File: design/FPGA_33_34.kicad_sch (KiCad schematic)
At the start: 21 parts, among them Q15 SI1036X, U1 XC7K160T-2FFG676C, U42 TXS0108E

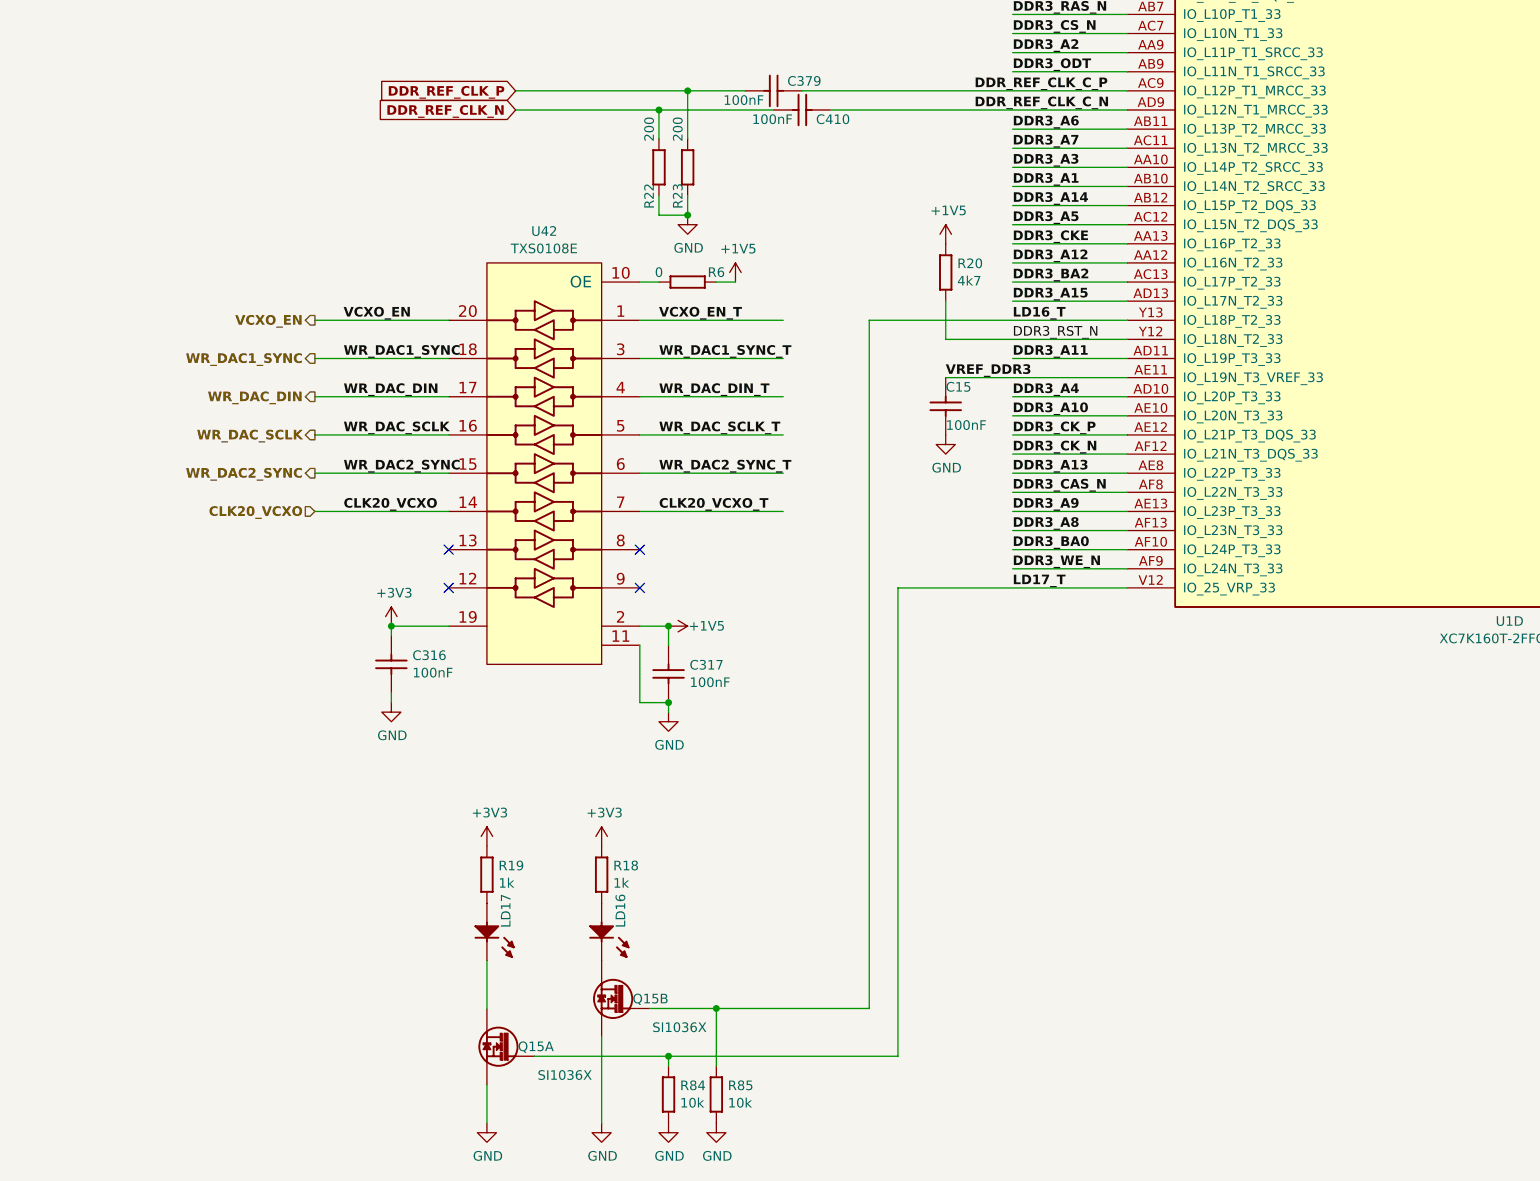
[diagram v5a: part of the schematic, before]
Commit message: new level translators
new level translators
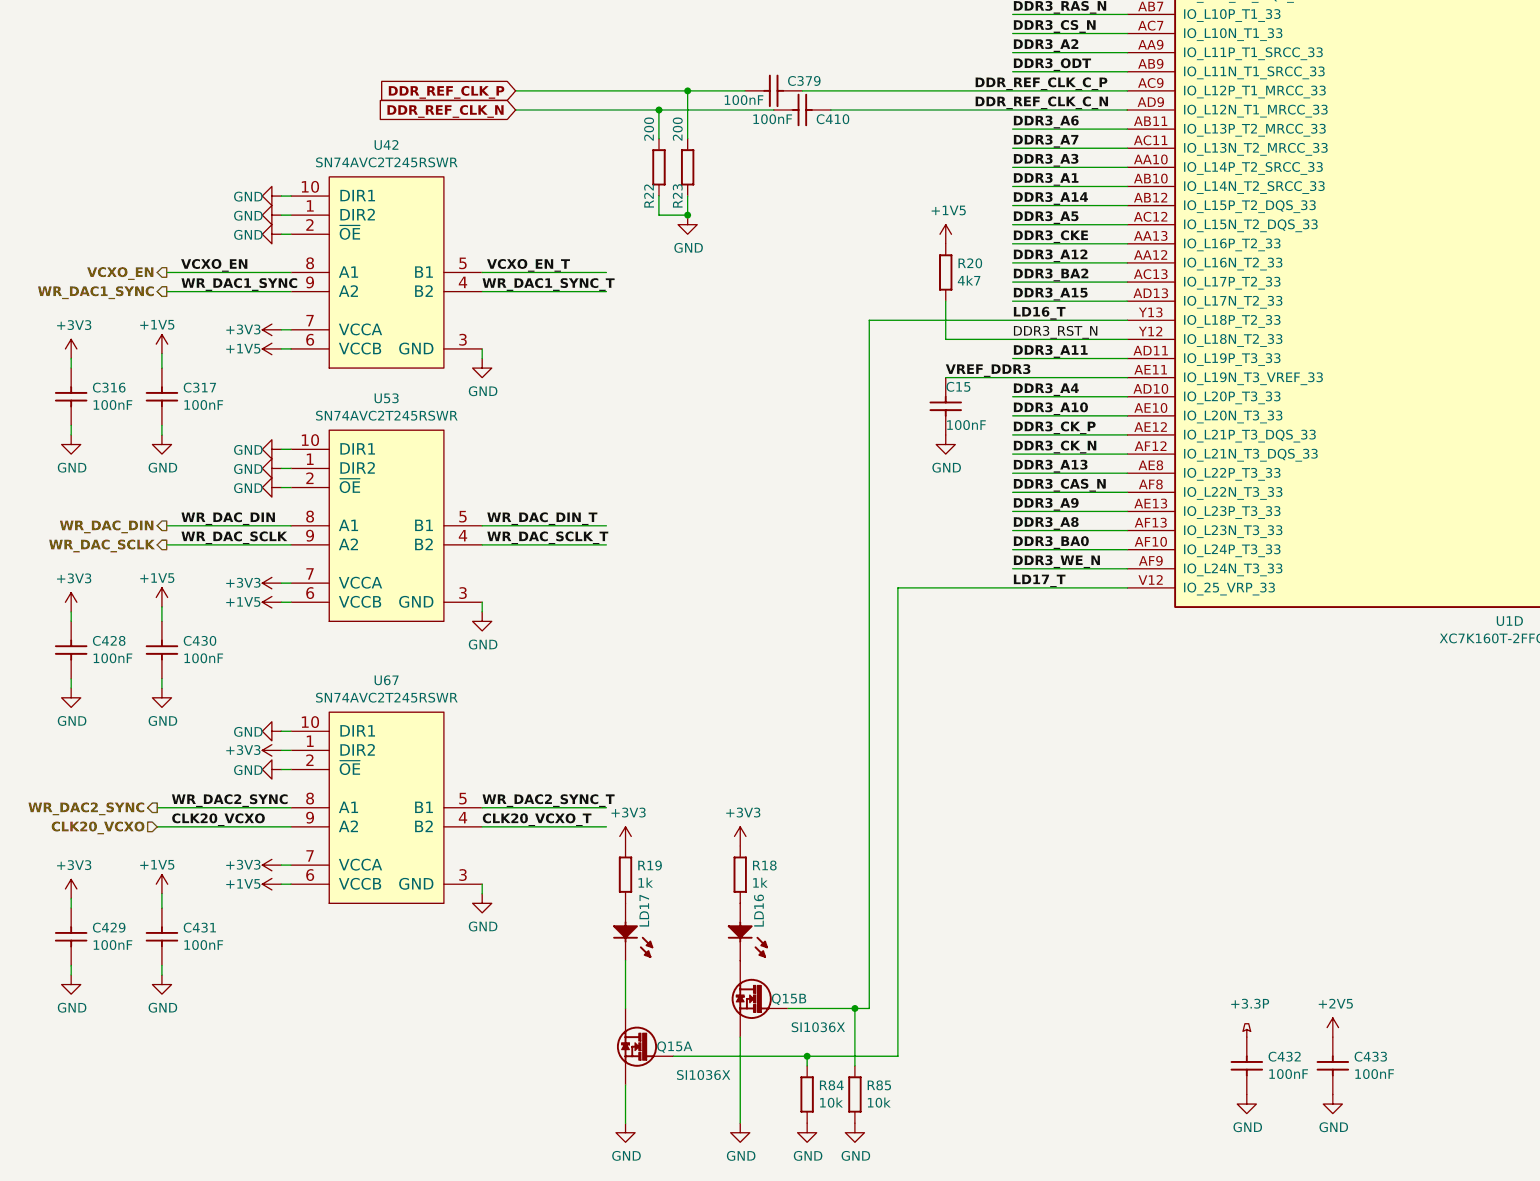
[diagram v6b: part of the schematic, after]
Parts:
- removed R6: R0402_0R_JUMPER, RESC1005X40N, symbol Resistors_SMD:R0402_0R_JUMPER
- removed U42: TXS0108E, ICs And Semiconductors SMD:SOP65P640X120-20N, symbol Analog_&_Interface:TXB0108PW
- added C428, C429, C430, C431, C432, C433: CC0201_100NF_6.3V_10%_X5R, CAPC0603X33N, symbol Capacitors_SMD:CC0201_100NF_6.3V_10%_X5R
- added U42, U53, U67: SN74AVC2T245RSWR, ICs And Semiconductors SMD:QFN40P140X180X55-10N, symbol Standard_Logic:SN74AVC2T245RSWR
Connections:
- net +1V5: now also C430.1, C431.1, U42.6 (VCCB), U53.6 (VCCB), U67.6 (VCCB)
- net +3V3: now also C428.1, C429.1, U42.7 (VCCA), U53.7 (VCCA), U67.1 (DIR2), U67.7 (VCCA)
- net CLK20_VCXO: now also U67.9 (A2)
- net CLK20_VCXO_T: now also U67.4 (B2)
- net GND: now also C428.2, C429.2, C430.2, C431.2, C432.2, C433.2, U42.1 (DIR2), U42.10 (DIR1), U42.2 (~{OE}), U42.3 (GND), U53.1 (DIR2), U53.10 (DIR1), U53.2 (~{OE}), U53.3 (GND), U67.10 (DIR1), U67.2 (~{OE}), U67.3 (GND)
- net VCXO_EN: now also U42.8 (A1)
- net VCXO_EN_T: now also U42.5 (B1)
- net WR_DAC1_SYNC: now also U42.9 (A2)
- net WR_DAC1_SYNC_T: now also U42.4 (B2)
- net WR_DAC2_SYNC: now also U67.8 (A1)
- net WR_DAC2_SYNC_T: now also U67.5 (B1)
- net WR_DAC_DIN: now also U53.8 (A1)
- net WR_DAC_DIN_T: now also U53.5 (B1)
- net WR_DAC_SCLK: now also U53.9 (A2)
- net WR_DAC_SCLK_T: now also U53.4 (B2)
- new net +2V5: C433.1
- new net +3.3P: C432.1
- no-connect marks 10 -> 6
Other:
- moved on the sheet: C316, C317, LD16, LD17, Q15A, Q15B, R18, R19, R84, R85

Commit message: routing done, no DRC errors
routing done, no DRC errors
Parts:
- removed C432, C433: CC0201_100NF_6.3V_10%_X5R, CAPC0603X33N, symbol Capacitors_SMD:CC0201_100NF_6.3V_10%_X5R
